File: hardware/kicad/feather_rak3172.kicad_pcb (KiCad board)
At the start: 2 copper layers, 51 x 23.1 mm, 51 parts, among them J1 Pin Header, J2 Pin Header, J3 USB_C_Receptacle_USB2.0, J4 915MHz SMA, J5 SWD, J6 JST-2PH, Q1 DMG341, SW1 RESET, SW2 BOOT, U1 RAK3172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

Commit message: remove 3v3 signal from swd pinout
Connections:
- J5 pad 1: +3V3 -> unconnected-(J5-Pad1)
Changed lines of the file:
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@@
   (net 29 "Net-(J3-PadB5)")
   (net 30 "unconnected-(J3-PadB8)")
-  (net 31 "+3V3")
+  (net 31 "unconnected-(J5-Pad1)")
   (net 32 "unconnected-(J5-Pad6)")
   (net 33 "Net-(R5-Pad1)")
@@
     (pad "" np_thru_hole circle (at 2.54 1.016 90) (size 0.9906 0.9906) (drill 0.9906) (layers *.Cu *.Mask))
     (pad "1" connect circle (at -1.27 -0.635 90) (size 0.7874 0.7874) (layers "B.Cu" "B.Mask")
-      (net 31 "+3V3") (pinfunction "Pin_1") (pintype "passive"))
+      (net 31 "unconnected-(J5-Pad1)") (pinfunction "Pin_1") (pintype "passive+no_connect"))
     (pad "2" connect circle (at -1.27 0.635 90) (size 0.7874 0.7874) (layers "B.Cu" "B.Mask")
       (net 43 "/PA13") (pinfunction "Pin_2") (pintype "passive"))

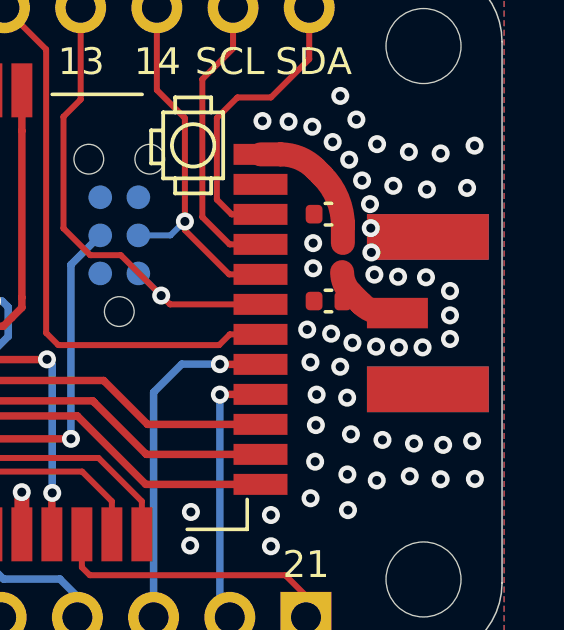
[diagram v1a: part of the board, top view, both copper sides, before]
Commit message: remove gnd via under antenna port
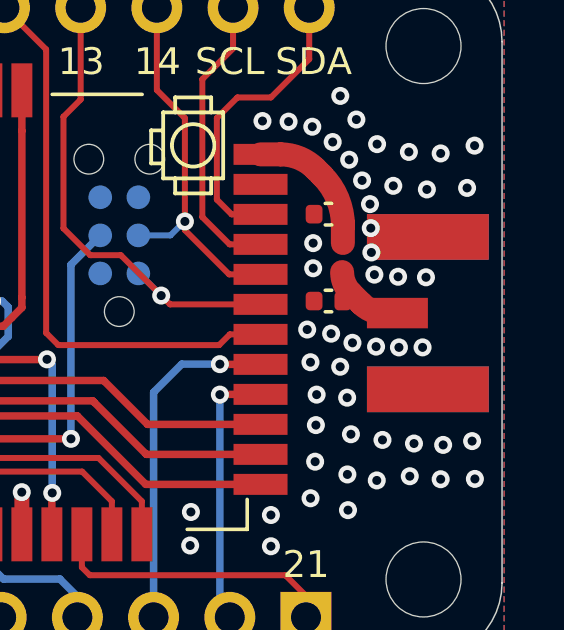
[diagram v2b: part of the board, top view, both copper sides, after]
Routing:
- net GND: vias 117 -> 114
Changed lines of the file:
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@@
   (via (at 120 106.5) (size 0.6) (drill 0.3) (layers "F.Cu" "B.Cu") (free) (net 1))
   (via (at 162.97 95.91) (size 0.6) (drill 0.3) (layers "F.Cu" "B.Cu") (free) (net 1))
-  (via (at 166.0906 103.2256) (size 0.6) (drill 0.3) (layers "F.Cu" "B.Cu") (free) (net 1))
   (via (at 127 111.633) (size 0.6) (drill 0.3) (layers "F.Cu" "B.Cu") (free) (net 1))
   (via (at 129.54 111.633) (size 0.6) (drill 0.3) (layers "F.Cu" "B.Cu") (free) (net 1))
@@
   (via (at 161.6202 106.0958) (size 0.6) (drill 0.3) (layers "F.Cu" "B.Cu") (free) (net 1))
   (via (at 126.492 92.202) (size 0.6) (drill 0.3) (layers "F.Cu" "B.Cu") (free) (net 1))
-  (via (at 166.0906 102.4382) (size 0.6) (drill 0.3) (layers "F.Cu" "B.Cu") (free) (net 1))
   (via (at 163.57 101.08) (size 0.6) (drill 0.3) (layers "F.Cu" "B.Cu") (free) (net 1))
   (via (at 162.69 108.93) (size 0.6) (drill 0.3) (layers "F.Cu" "B.Cu") (free) (net 1))
@@
   (via (at 166.66 98.19) (size 0.6) (drill 0.3) (layers "F.Cu" "B.Cu") (free) (net 1))
   (via (at 162.1282 103.0478) (size 0.6) (drill 0.3) (layers "F.Cu" "B.Cu") (free) (net 1))
-  (via (at 166.0906 101.6254) (size 0.6) (drill 0.3) (layers "F.Cu" "B.Cu") (free) (net 1))
   (via (at 161.44 104) (size 0.6) (drill 0.3) (layers "F.Cu" "B.Cu") (free) (net 1))
   (via (at 144.8054 109.0676) (size 0.6) (drill 0.3) (layers "F.Cu" "B.Cu") (free) (net 1))

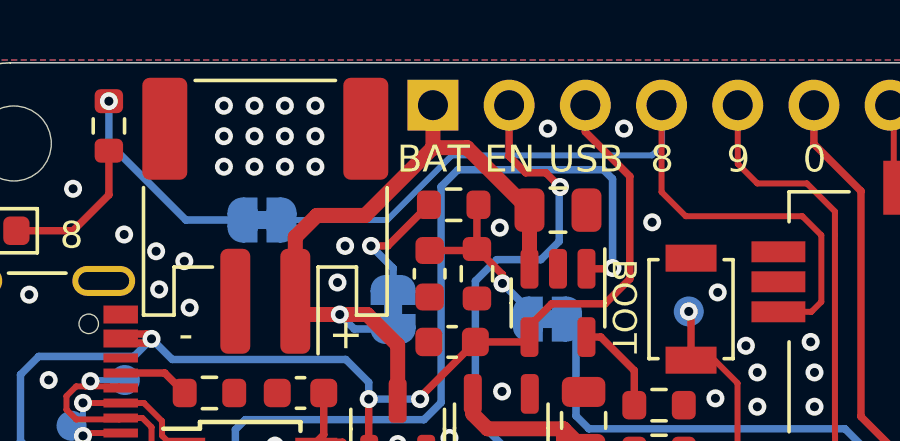
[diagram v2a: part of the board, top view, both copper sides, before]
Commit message: add extra trace to batt pin out
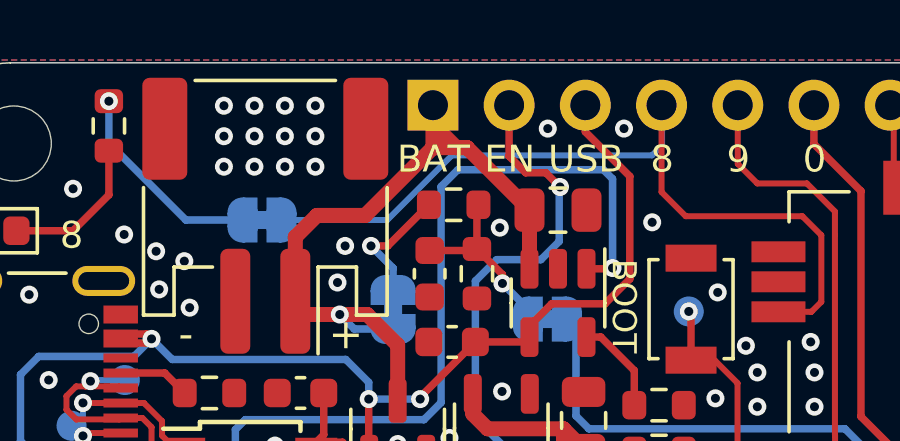
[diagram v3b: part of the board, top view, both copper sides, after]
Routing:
- net +BATT: track 23.3 -> 24.7 mm
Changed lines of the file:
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@@
   (segment (start 136.75552 109.37048) (end 124.94452 109.37048) (width 0.25) (layer "B.Cu") (net 13))
   (segment (start 153.4563 100.7469) (end 154.432 99.7712) (width 0.25) (layer "B.Cu") (net 13))
+  (segment (start 134.59601 93.60041) (end 134.24041 93.60041) (width 0.5) (layer "F.Cu") (net 14))
   (segment (start 131.2672 99.1616) (end 130.3528 99.1616) (width 0.5) (layer "F.Cu") (net 14))
+  (segment (start 133.458949 92.183949) (end 133.458949 92.818949) (width 0.5) (layer "F.Cu") (net 14))
   (segment (start 129.3126 99.1616) (end 128.8709 98.7199) (width 0.25) (layer "F.Cu") (net 14))
   (segment (start 128.8709 96.5795) (end 128.8709 98.7199) (width 0.5) (layer "F.Cu") (net 14))
   (segment (start 136.6774 97.6376) (end 136.6774 95.6818) (width 0.5) (layer "F.Cu") (net 14))
-  (segment (start 133.458949 92.183949) (end 133.458949 93.60041) (width 0.5) (layer "F.Cu") (net 14))
+  (segment (start 134.24041 93.60041) (end 133.458949 92.818949) (width 0.5) (layer "F.Cu") (net 14))
+  (segment (start 133.458949 92.818949) (end 133.458949 93.60041) (width 0.5) (layer "F.Cu") (net 14))
   (segment (start 136.6774 95.6818) (end 134.59601 93.60041) (width 0.5) (layer "F.Cu") (net 14))
   (segment (start 132.2832 100.1776) (end 131.2672 99.1616) (width 0.5) (layer "F.Cu") (net 14))

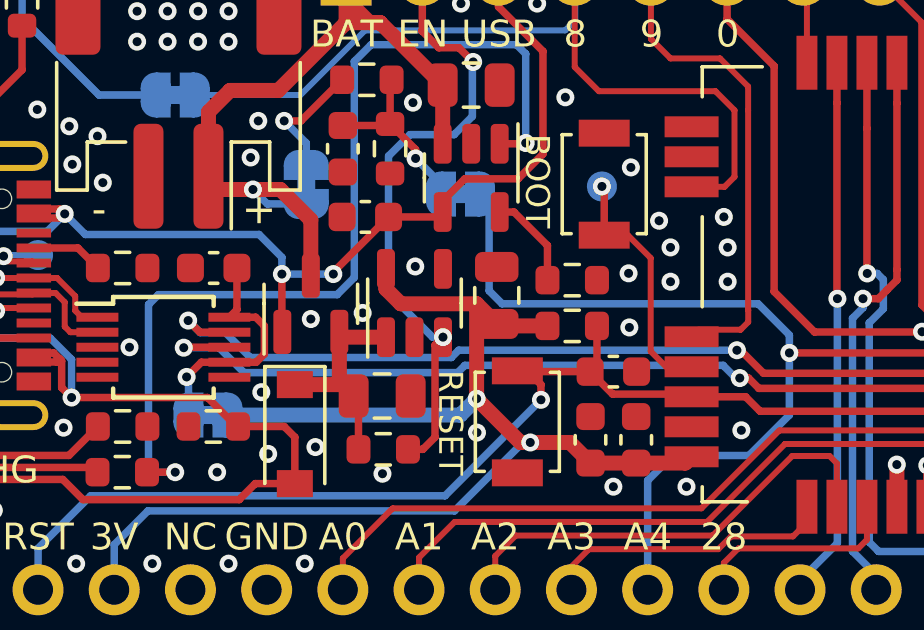
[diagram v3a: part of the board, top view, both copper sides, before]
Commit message: add solder jump for txd and rxd, minor silkscreen changes
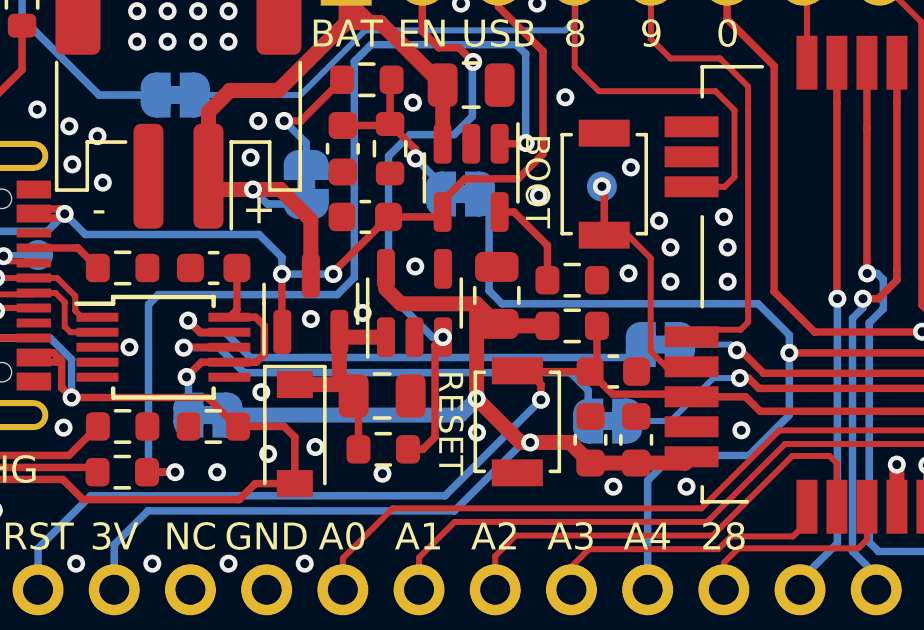
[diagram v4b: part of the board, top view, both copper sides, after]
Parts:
- added JP5: ENTXD, Jumper:SolderJumper-2_P1.3mm_Bridged_RoundedPad1.0x1.5mm, B.Cu at (142.2, 106.9)
- added JP6: ENRXD, Jumper:SolderJumper-2_P1.3mm_Bridged_RoundedPad1.0x1.5mm, B.Cu at (143.9, 104.3)
- moved G*** 2.35 mm to (147.7, 100.0)
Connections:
- U2 pad 8: /RXD2 -> Net-(U2-Pad8)
- U2 pad 9: /TXD2 -> Net-(U2-Pad9)
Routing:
- net /TXD2: track 34.8 -> 16.3 mm, vias 2 -> 1
- net Net-(U2-Pad9): track 0.00 -> 17.3 mm, vias 0 -> 1
- net Net-(U2-Pad8): track 0.00 -> 16.6 mm, vias 0 -> 1
- net /RXD2: track 35.0 -> 18.6 mm, vias 2 -> 1
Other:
- board text added: "10"
- board text added: "15"
- board text added: "18"
- board text added: "19"
- board text added: "20"
- board text added: "Rev 8"
- board text added: "SCL/12"
- board text added: "SDA/11"
- board text removed: "10/A3"
- board text removed: "11/SDA"
- board text removed: "12/SCL"
- board text removed: "15/A4"
- board text removed: "18/A2"
- board text removed: "19/A0"
- board text removed: "20/A1"
- board text removed: "Rev 7"

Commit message: minor silkscreen changes
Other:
- board text added: "Rev 8.1"
- board text removed: "Rev 8"
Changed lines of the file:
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@@
       (effects (font (size 0.5 0.5) (thickness 0.125)) (justify mirror))
     )
-    (fp_text value "BOOT" (at 2.032 1.778 180) (layer "B.SilkS")
+    (fp_text value "BOOT" (at 1.651 1.524 180) (layer "B.SilkS")
       (effects (font (size 0.8 0.8) (thickness 0.15)) (justify mirror))
     )
@@
     (effects (font (size 0.89408 0.89408) (thickness 0.15)) (justify mirror))
   )
-  (gr_text "Rev 8" (at 128.524 104.648) (layer "B.SilkS")
+  (gr_text "Rev 8.1" (at 128.524 104.648) (layer "B.SilkS")
     (effects (font (size 0.8 0.8) (thickness 0.1)) (justify mirror))
   )
